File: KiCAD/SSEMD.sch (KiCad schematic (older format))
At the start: 0 parts

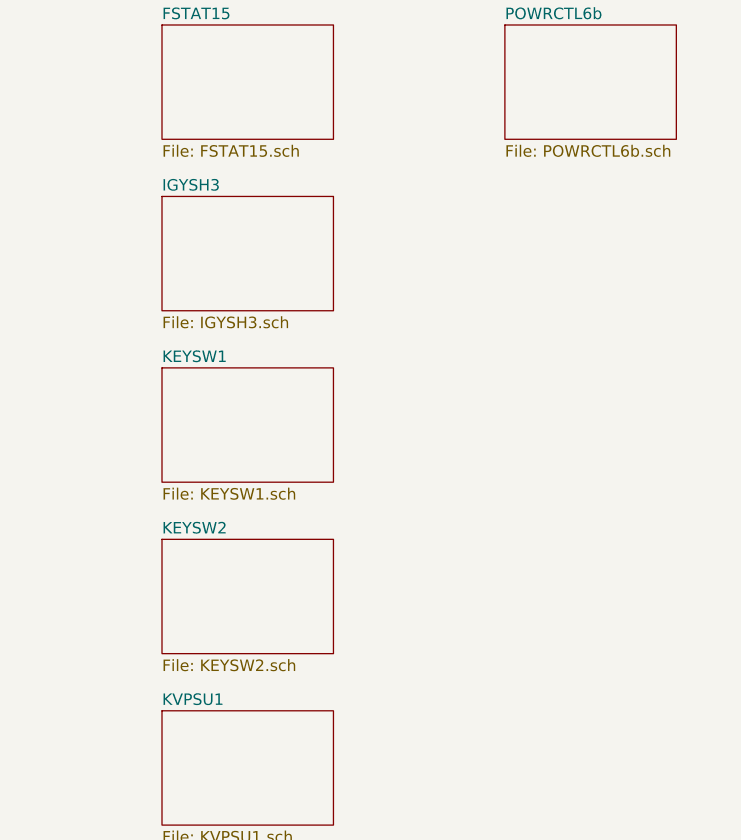
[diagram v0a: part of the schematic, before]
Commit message: Add Prepulse PSEPCTL RMONDRS.
Signed-off-by: John Bradley <flypie@rocketmail.com>
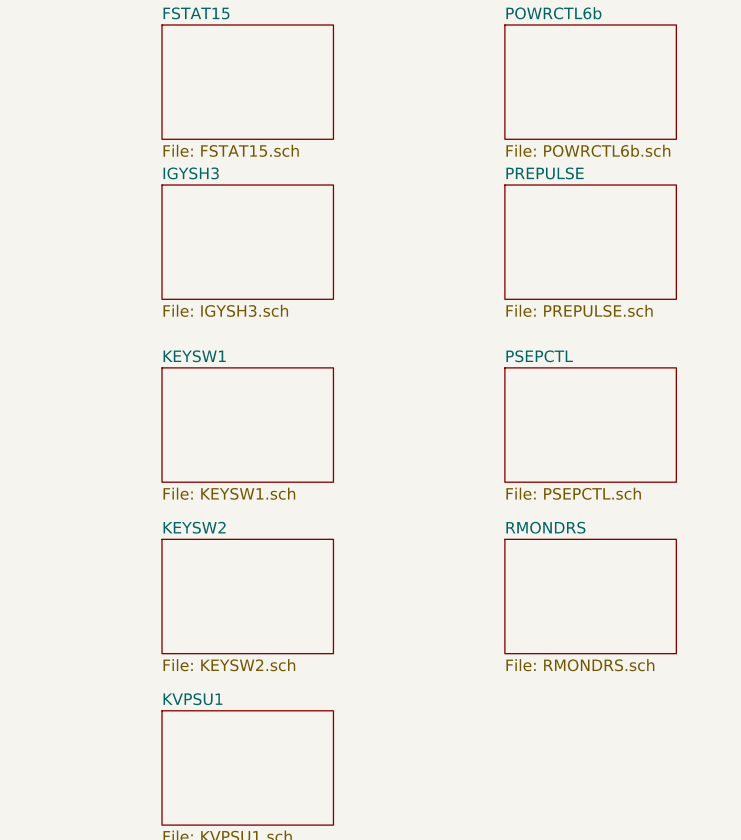
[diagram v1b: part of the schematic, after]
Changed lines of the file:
@@
 $Descr A4 11693 8268
 encoding utf-8
-Sheet 1 29
+Sheet 1 32
 Title "Control Adder Position 6.4"
 Date "2020-10-08"
@@
 $EndSheet
 $Sheet
-S 4000 1750 750  500
+S 4000 1700 750  500
 U 5F59FE33
 F0 "IGYSH3" 50
@@
 F1 "POWRCTL6b.sch" 50
 $EndSheet
+$Sheet
+S 5500 1700 750  500
+U 5F83BB04
+F0 "PREPULSE" 50
+F1 "PREPULSE.sch" 50
+$EndSheet
+$Sheet
+S 5500 2500 750  500
+U 5F873206
+F0 "PSEPCTL" 50
+F1 "PSEPCTL.sch" 50
+$EndSheet
+$Sheet
+S 5500 3250 750  500
+U 607AC010
+F0 "RMONDRS" 50
+F1 "RMONDRS.sch" 50
+$EndSheet
 $EndSCHEMATC

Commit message: Add scfollws.sch
Signed-off-by: John Bradley <flypie@rocketmail.com>
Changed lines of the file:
@@
 $Descr A4 11693 8268
 encoding utf-8
-Sheet 1 32
+Sheet 1 33
 Title "Control Adder Position 6.4"
 Date "2020-10-08"
@@
 F1 "RMONDRS.sch" 50
 $EndSheet
+$Sheet
+S 5500 4000 750  500
+U 5F868E46
+F0 "SCFOLLWS" 50
+F1 "SCFOLLWS.sch" 50
+$EndSheet
 $EndSCHEMATC

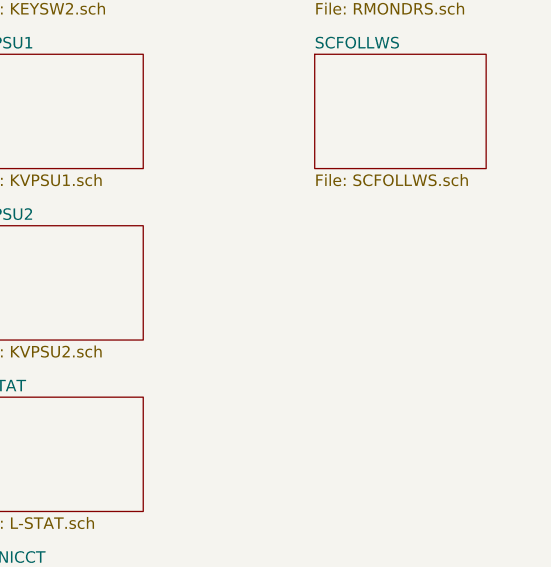
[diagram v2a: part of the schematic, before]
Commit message: Add sclock correct fault in ACGATE.
Signed-off-by: John Bradley <flypie@rocketmail.com>
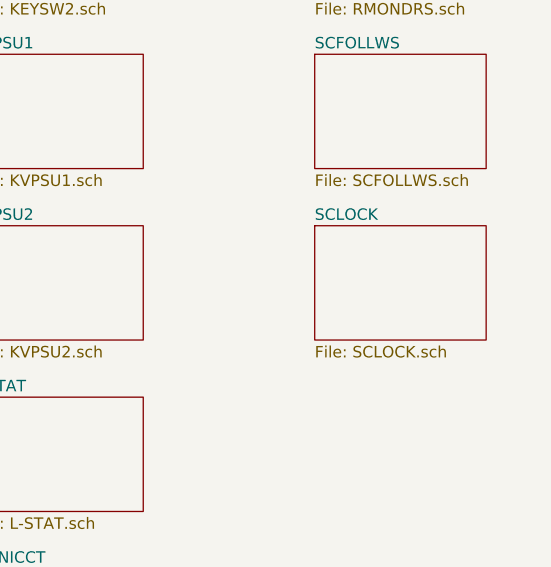
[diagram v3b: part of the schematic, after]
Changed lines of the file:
@@
 $Descr A4 11693 8268
 encoding utf-8
-Sheet 1 33
+Sheet 1 34
 Title "Control Adder Position 6.4"
 Date "2020-10-08"
@@
 F1 "SCFOLLWS.sch" 50
 $EndSheet
+$Sheet
+S 5500 4750 750  500
+U 60BC2C2A
+F0 "SCLOCK" 50
+F1 "SCLOCK.sch" 50
+$EndSheet
 $EndSCHEMATC

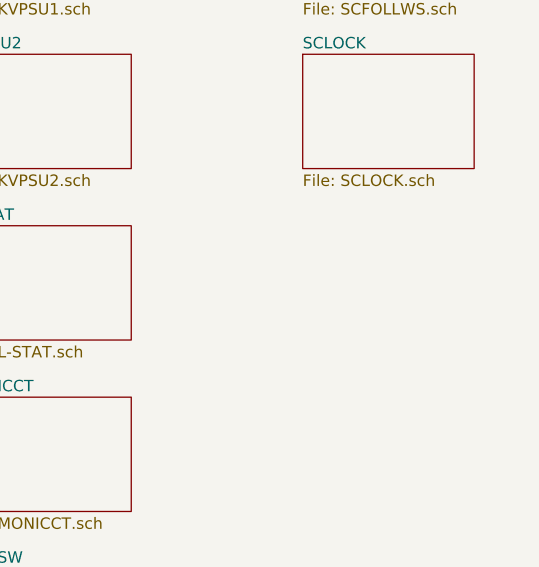
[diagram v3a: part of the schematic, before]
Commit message: Add SDOT&STB.
Signed-off-by: John Bradley <flypie@rocketmail.com>
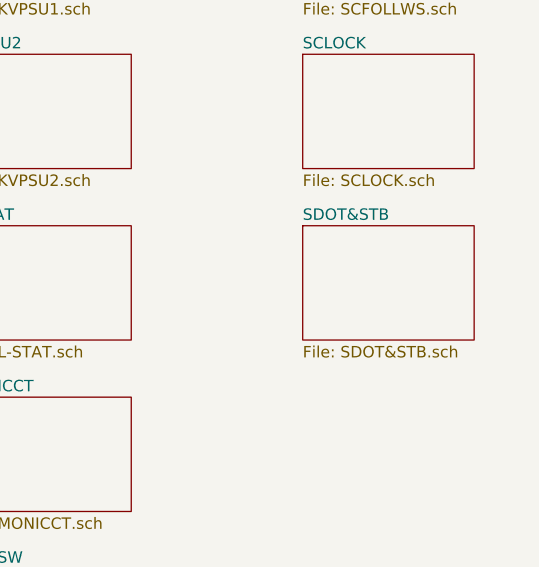
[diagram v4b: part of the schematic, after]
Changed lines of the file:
@@
 $Descr A4 11693 8268
 encoding utf-8
-Sheet 1 34
+Sheet 1 35
 Title "Control Adder Position 6.4"
 Date "2020-10-08"
@@
 F1 "SCLOCK.sch" 50
 $EndSheet
+$Sheet
+S 5500 5500 750  500
+U 5F89117E
+F0 "SDOT&STB" 50
+F1 "SDOT&STB.sch" 50
+$EndSheet
 $EndSCHEMATC

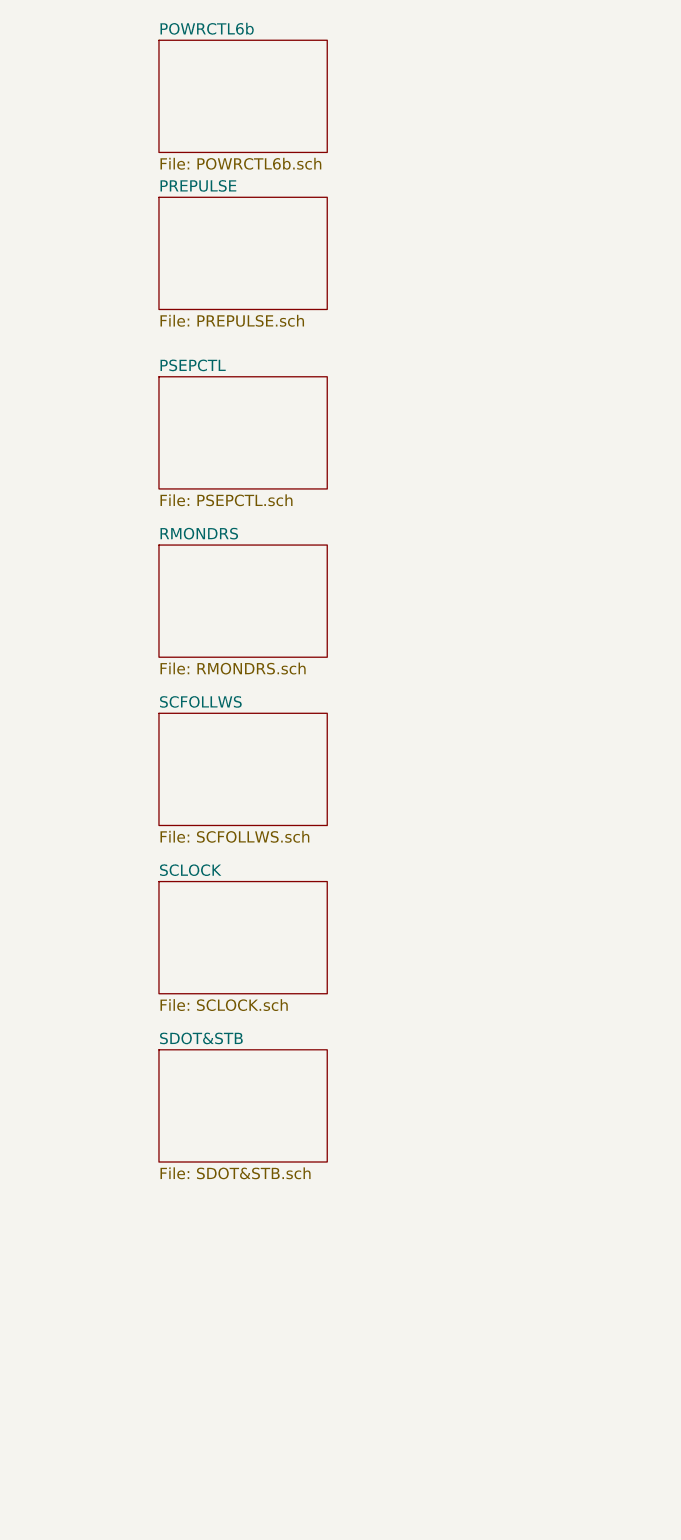
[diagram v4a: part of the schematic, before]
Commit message: Add sclock, sdot&stb smonxtb
Signed-off-by: John Bradley <flypie@rocketmail.com>
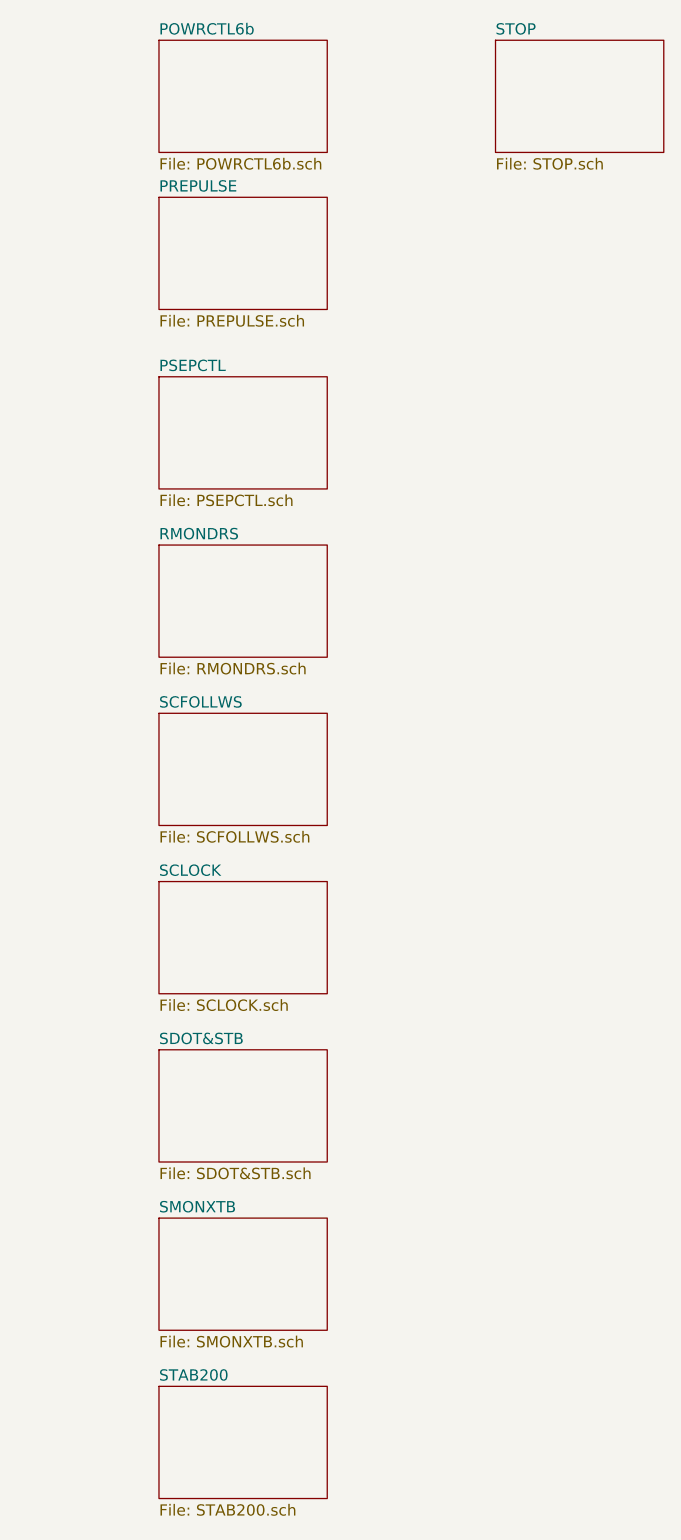
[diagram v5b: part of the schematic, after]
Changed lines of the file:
@@
 $Descr A4 11693 8268
 encoding utf-8
-Sheet 1 35
+Sheet 1 38
 Title "Control Adder Position 6.4"
 Date "2020-10-08"
@@
 F1 "SDOT&STB.sch" 50
 $EndSheet
+$Sheet
+S 5500 6250 750  500
+U 5F88E8BA
+F0 "SMONXTB" 50
+F1 "SMONXTB.sch" 50
+$EndSheet
+$Sheet
+S 5500 7000 750  500
+U 6077FCA5
+F0 "STAB200" 50
+F1 "STAB200.sch" 50
+$EndSheet
+$Sheet
+S 7000 1000 750  500
+U 5F89590E
+F0 "STOP" 50
+F1 "STOP.sch" 50
+$EndSheet
 $EndSCHEMATC

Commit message: Add StorGate & some Valve Logic data.
Signed-off-by: John Bradley <flypie@rocketmail.com>
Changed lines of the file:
@@
 $Descr A4 11693 8268
 encoding utf-8
-Sheet 1 38
+Sheet 1 39
 Title "Control Adder Position 6.4"
 Date "2020-10-08"
@@
 F1 "STOP.sch" 50
 $EndSheet
+$Sheet
+S 7000 1750 750  450
+U 5FFFB333
+F0 "STORGATE" 50
+F1 "STORGATE.sch" 50
+$EndSheet
 $EndSCHEMATC

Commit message: Add SUBTR1.sch, SXTMBASE.sch TRANSFER.sch.
Signed-off-by: John Bradley <flypie@rocketmail.com>
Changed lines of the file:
@@
 $Descr A4 11693 8268
 encoding utf-8
-Sheet 1 39
+Sheet 1 42
 Title "Control Adder Position 6.4"
 Date "2020-10-08"
@@
 F1 "STORGATE.sch" 50
 $EndSheet
+$Sheet
+S 7000 2500 750  500
+U 5FEEBA24
+F0 "SUBTR1" 50
+F1 "SUBTR1.sch" 50
+$EndSheet
+$Sheet
+S 7000 3250 750  500
+U 5FD26B52
+F0 "SXTMBASE" 50
+F1 "SXTMBASE.sch" 50
+$EndSheet
+$Sheet
+S 7000 4000 750  500
+U 642F1647
+F0 "TRANSFER" 50
+F1 "TRANSFER.sch" 50
+$EndSheet
 $EndSCHEMATC

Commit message: Add TYPEWE WRERCCTS YAMP&HVR.
Which com,pletes the first pass. All the pages are done but I haven't checked them yet and there are bound to be errosr.

Signed-off-by: John Bradley <flypie@rocketmail.com>
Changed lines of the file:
@@
 $Descr A4 11693 8268
 encoding utf-8
-Sheet 1 42
+Sheet 1 45
 Title "Control Adder Position 6.4"
 Date "2020-10-08"
@@
 F1 "TRANSFER.sch" 50
 $EndSheet
+$Sheet
+S 7000 4750 800  500
+U 5F8FF235
+F0 "TYPEWR" 50
+F1 "TYPEWR.sch" 50
+$EndSheet
+$Sheet
+S 7000 5500 800  500
+U 5F9BDCBE
+F0 "WRERCCTS" 50
+F1 "WRERCCTS.sch" 50
+$EndSheet
+$Sheet
+S 8500 1000 750  500
+U 62085011
+F0 "YAMP&HVR" 50
+F1 "YAMP&HVR.sch" 50
+$EndSheet
 $EndSCHEMATC
